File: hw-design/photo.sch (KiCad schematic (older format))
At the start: 10 parts, among them P6 CONN_01X17, P7 CONN_01X17, Q1 BC847, U2 TCS3472, U9 TCS3472

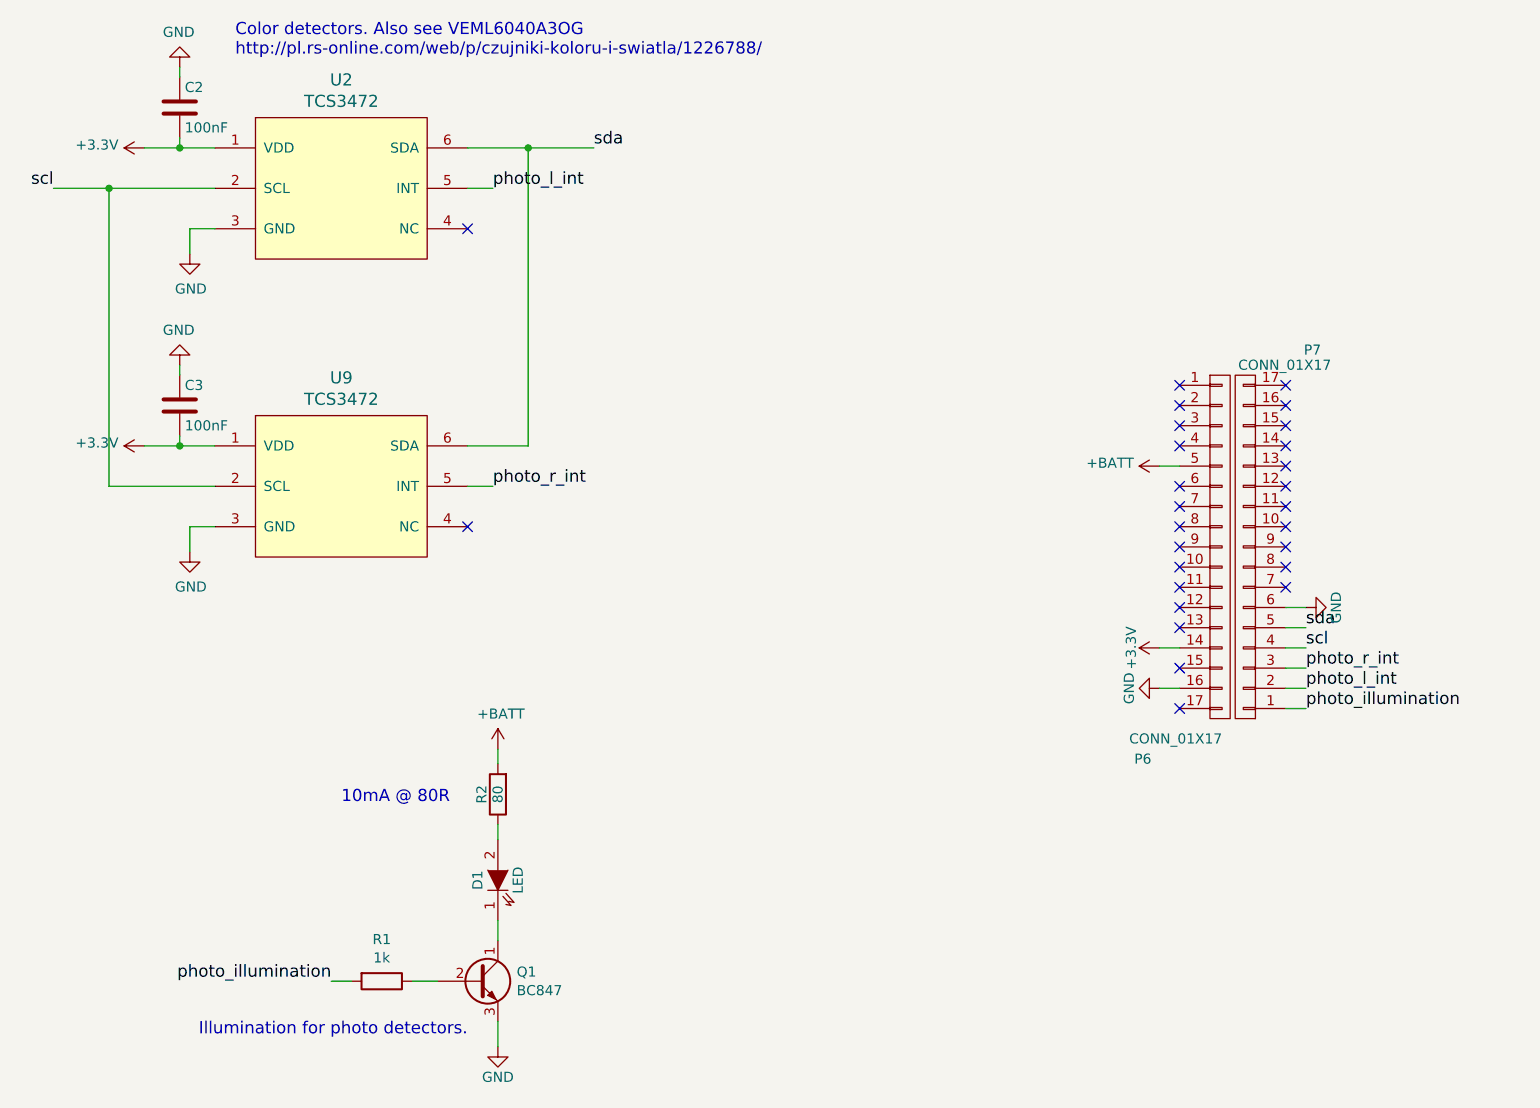
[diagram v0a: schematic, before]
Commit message: 2 boards and 1 little with color sensors.
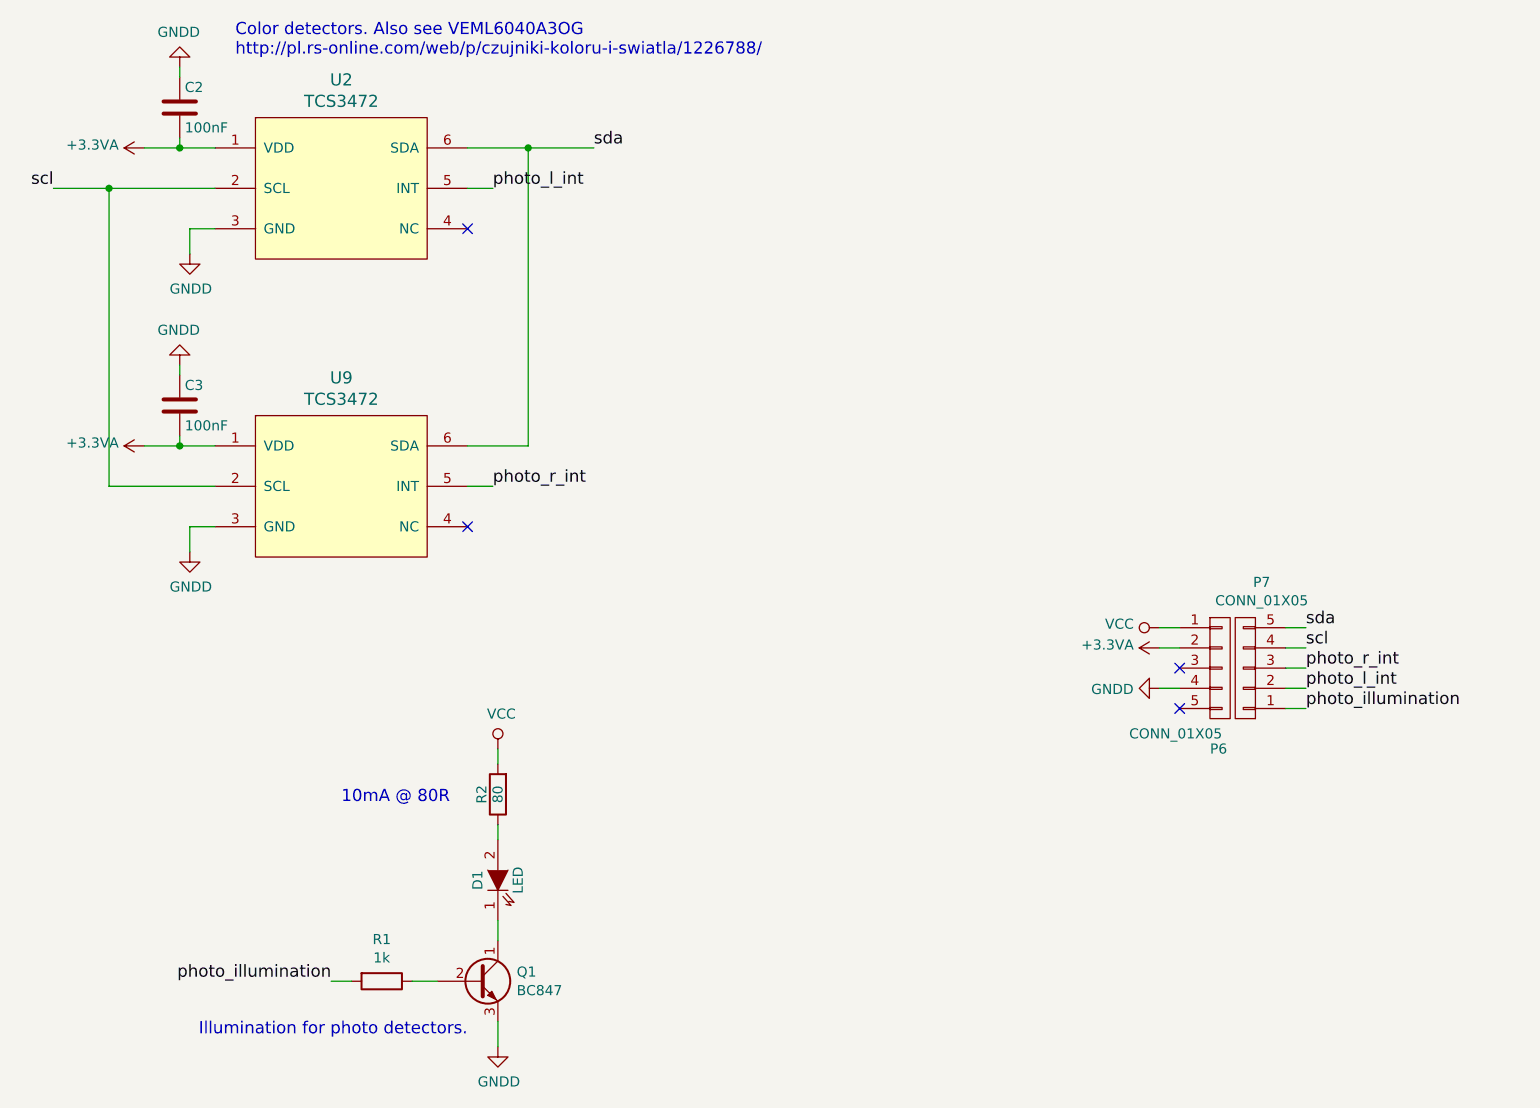
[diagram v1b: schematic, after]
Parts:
- removed P6, P7: CONN_01X17, iwasz:pin_socket_17, symbol CONN_01X17
- added P6, P7: CONN_01X05, w_pin_strip:pin_strip_5, symbol CONN_01X05
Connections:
- net photo_illumination: now also P7.1 (P1)
- net photo_l_int: now also P7.2 (P2)
- net photo_r_int: now also P7.3 (P3)
- net scl: now also P7.4 (P4)
- net sda: now also P7.5 (P5)
- net +3V3 renamed +3.3VA
- net +3.3VA: now also P6.2 (P2)
- net +BATT renamed VCC
- net VCC: now also P6.1 (P1)
- net GND renamed GNDD
- net GNDD: now also P6.4 (P4)
- no-connect marks 27 -> 4
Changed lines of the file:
@@
-	1    0    0    -1
-$EndComp
-$Comp
-L +3.3V #PWR72
-U 1 1 580FD812
-P 1625 1800
-F 0 "#PWR72" H 1625 1650 50  0001 C CNN
-F 1 "+3.3V" V 1640 1928 50  0000 L CNN
-F 2 "" H 1625 1800 50  0000 C CNN
-F 3 "" H 1625 1800 50  0000 C CNN
-	1    1625 1800
-	0    -1   -1   0
-$EndComp
-$Comp
-L GND #PWR74
-U 1 1 580FD818
-P 1800 1400
-F 0 "#PWR74" H 1800 1150 50  0001 C CNN
-F 1 "GND" H 1805 1227 50  0000 C CNN
-F 2 "" H 1800 1400 50  0000 C CNN
-F 3 "" H 1800 1400 50  0000 C CNN
-	1    1800 1400
-	-1   0    0    1
-$EndComp
-$Comp
-L GND #PWR76
-U 1 1 580FD81E
-P 1850 2325
-F 0 "#PWR76" H 1850 2075 50  0001 C CNN
-F 1 "GND" H 1855 2152 50  0000 C CNN
-F 2 "" H 1850 2325 50  0000 C CNN
-F 3 "" H 1850 2325 50  0000 C CNN
-	1    1850 2325
 	1    0    0    -1
 $EndComp
@@
 	1    0    0    -1
 $EndComp
-$Comp
-L +3.3V #PWR73
-U 1 1 580FD837
-P 1625 3275
-F 0 "#PWR73" H 1625 3125 50  0001 C CNN
-F 1 "+3.3V" V 1640 3403 50  0000 L CNN
-F 2 "" H 1625 3275 50  0000 C CNN
-F 3 "" H 1625 3275 50  0000 C CNN
-	1    1625 3275
-	0    -1   -1   0
-$EndComp
-$Comp
-L GND #PWR75
-U 1 1 580FD83D
-P 1800 2875
-F 0 "#PWR75" H 1800 2625 50  0001 C CNN
-F 1 "GND" H 1805 2702 50  0000 C CNN
-F 2 "" H 1800 2875 50  0000 C CNN
-F 3 "" H 1800 2875 50  0000 C CNN
-	1    1800 2875
-	-1   0    0    1
-$EndComp
-$Comp
-L GND #PWR77
-U 1 1 580FD843
-P 1850 3800
-F 0 "#PWR77" H 1850 3550 50  0001 C CNN
-F 1 "GND" H 1855 3627 50  0000 C CNN
-F 2 "" H 1850 3800 50  0000 C CNN
-F 3 "" H 1850 3800 50  0000 C CNN
-	1    1850 3800
-	1    0    0    -1
-$EndComp
 NoConn ~ 3225 3675
 $Comp
@@
 	-1   0    0    1
 $EndComp
-$Comp
-L GND #PWR79
-U 1 1 580FD859
-P 3375 6250
-F 0 "#PWR79" H 3375 6000 50  0001 C CNN
-F 1 "GND" H 3375 6100 50  0000 C CNN
-F 2 "" H 3375 6250 60  0000 C CNN
-F 3 "" H 3375 6250 60  0000 C CNN
-	1    3375 6250
-	1    0    0    -1
-$EndComp
 Text Notes 2075 1350 0    60   ~ 0
 Color detectors. Also see VEML6040A3OG\nhttp://pl.rs-online.com/web/p/czujniki-koloru-i-swiatla/1226788/
@@
 Wire Wire Line
 	2550 5925 2650 5925
-$Comp
-L +BATT #PWR78
-U 1 1 580FD88C
-P 3375 4775
-F 0 "#PWR78" H 3375 4625 50  0001 C CNN
-F 1 "+BATT" H 3390 4948 50  0000 C CNN
-F 2 "" H 3375 4775 50  0000 C CNN
-F 3 "" H 3375 4775 50  0000 C CNN
-	1    3375 4775
-	1    0    0    -1
-$EndComp
 Text Notes 2600 5050 0    60   ~ 0
 10mA @ 80R
-$Comp
-L GND #PWR82
-U 1 1 580FEB92
-P 6650 4475
-F 0 "#PWR82" H 6650 4225 50  0001 C CNN
-F 1 "GND" H 6650 4325 50  0000 C CNN
-F 2 "" H 6650 4475 60  0000 C CNN
-F 3 "" H 6650 4475 60  0000 C CNN
-	1    6650 4475
-	0    1    1    0
-$EndComp
-$Comp
-L +3.3V #PWR81
-U 1 1 580FEB98
-P 6650 4275
-F 0 "#PWR81" H 6650 4125 50  0001 C CNN
-F 1 "+3.3V" H 6650 4415 50  0000 C CNN
-F 2 "" H 6650 4275 60  0000 C CNN
-F 3 "" H 6650 4275 60  0000 C CNN
-	1    6650 4275
-	0    -1   -1   0
-$EndComp
-$Comp
-L +BATT #PWR80
-U 1 1 580FEB9E
-P 6650 3375
-F 0 "#PWR80" H 6650 3225 50  0001 C CNN
-F 1 "+BATT" V 6665 3502 50  0000 L CNN
-F 2 "" H 6650 3375 50  0000 C CNN
-F 3 "" H 6650 3375 50  0000 C CNN
-	1    6650 3375
-	0    -1   -1   0
-$EndComp
-$Comp
-L CONN_01X17 P6
-U 1 1 580FEBAA
-P 6950 3775
-F 0 "P6" H 6525 2725 50  0000 L CNN
-F 1 "CONN_01X17" H 6500 2825 50  0000 L CNN
-F 2 "iwasz:pin_socket_17" H 6950 3775 50  0001 C CNN
-F 3 "" H 6950 3775 50  0000 C CNN
-	1    6950 3775
-	1    0    0    -1
-$EndComp
-$Comp
-L CONN_01X17 P7
-U 1 1 580FEBB1
-P 7075 3775
-F 0 "P7" H 6700 2800 50  0000 L CNN
-F 1 "CONN_01X17" H 6650 2875 50  0000 L CNN
-F 2 "iwasz:pin_socket_17" H 7075 3775 50  0001 C CNN
-F 3 "" H 7075 3775 50  0000 C CNN
-	1    7075 3775
-	-1   0    0    1
-$EndComp
-$Comp
-L GND #PWR83
-U 1 1 580FEBB8
-P 7375 4075
-F 0 "#PWR83" H 7375 3825 50  0001 C CNN
-F 1 "GND" H 7375 3925 50  0000 C CNN
-F 2 "" H 7375 4075 60  0000 C CNN
-F 3 "" H 7375 4075 60  0000 C CNN
-	1    7375 4075
-	0    -1   -1   0
-$EndComp
 Wire Wire Line
 	7375 4575 7275 4575
@@
 	7275 4175 7375 4175
 Wire Wire Line
-	7375 4075 7275 4075
-Wire Wire Line
 	6650 4475 6750 4475
 Wire Wire Line
 	6650 4275 6750 4275
-Wire Wire Line
-	6650 3375 6750 3375
 Text Label 2550 5925 2    60   ~ 0
 photo_illumination
-NoConn ~ 7275 2975
-NoConn ~ 7275 3075
-NoConn ~ 7275 3175
-NoConn ~ 7275 3275
-NoConn ~ 7275 3375
-NoConn ~ 7275 3475
-NoConn ~ 7275 3575
-NoConn ~ 7275 3675
-NoConn ~ 7275 3775
-NoConn ~ 7275 3875
-NoConn ~ 7275 3975
-NoConn ~ 6750 2975
-NoConn ~ 6750 3075
-NoConn ~ 6750 3175
-NoConn ~ 6750 3275
-NoConn ~ 6750 3475
-NoConn ~ 6750 3575
-NoConn ~ 6750 3675
-NoConn ~ 6750 3775
-NoConn ~ 6750 3875
-NoConn ~ 6750 3975
-NoConn ~ 6750 4075
-NoConn ~ 6750 4175
 NoConn ~ 6750 4375
 NoConn ~ 6750 4575
@@
 Text Label 3850 1800 0    60   ~ 0
 sda
+Wire Wire Line
+	6650 4175 6750 4175
+$Comp
+L CONN_01X05 P6
+U 1 1 58107EC9
+P 6950 4375
+F 0 "P6" H 6900 3975 50  0000 L CNN
+F 1 "CONN_01X05" H 6500 4050 50  0000 L CNN
+F 2 "w_pin_strip:pin_strip_5" H 6950 4375 50  0001 C CNN
+F 3 "" H 6950 4375 50  0000 C CNN
+	1    6950 4375
+	1    0    0    -1
+$EndComp
+$Comp
+L CONN_01X05 P7
+U 1 1 58107F52
+P 7075 4375
+F 0 "P7" H 6994 3950 50  0000 C CNN
+F 1 "CONN_01X05" H 6994 4041 50  0000 C CNN
+F 2 "w_pin_strip:pin_strip_5" H 7075 4375 50  0001 C CNN
+F 3 "" H 7075 4375 50  0000 C CNN
+	1    7075 4375
+	-1   0    0    1
+$EndComp
+$Comp
+L GNDD #PWR072
+U 1 1 5810AACC
+P 6650 4475
+F 0 "#PWR072" H 6650 4225 50  0001 C CNN
+F 1 "GNDD" V 6655 4347 50  0000 R CNN
+F 2 "" H 6650 4475 50  0000 C CNN
+F 3 "" H 6650 4475 50  0000 C CNN
+	1    6650 4475
+	0    1    1    0
+$EndComp
+$Comp
+L GNDD #PWR073
+U 1 1 5810ACB5
+P 3375 6250
+F 0 "#PWR073" H 3375 6000 50  0001 C CNN
+F 1 "GNDD" H 3380 6077 50  0000 C CNN
+F 2 "" H 3375 6250 50  0000 C CNN
+F 3 "" H 3375 6250 50  0000 C CNN
+	1    3375 6250
+	1    0    0    -1
+$EndComp
+$Comp
+L GNDD #PWR074
+U 1 1 5810AE79
+P 1850 3800
+F 0 "#PWR074" H 1850 3550 50  0001 C CNN
+F 1 "GNDD" H 1855 3627 50  0000 C CNN
+F 2 "" H 1850 3800 50  0000 C CNN
+F 3 "" H 1850 3800 50  0000 C CNN
+	1    1850 3800
+	1    0    0    -1
+$EndComp
+$Comp
+L GNDD #PWR075
+U 1 1 5810B1A5
+P 1850 2325
+F 0 "#PWR075" H 1850 2075 50  0001 C CNN
+F 1 "GNDD" H 1855 2152 50  0000 C CNN
+F 2 "" H 1850 2325 50  0000 C CNN
+F 3 "" H 1850 2325 50  0000 C CNN
+	1    1850 2325
+	1    0    0    -1
+$EndComp
+$Comp
+L GNDD #PWR076
+U 1 1 5810BAE3
+P 1800 1400
+F 0 "#PWR076" H 1800 1150 50  0001 C CNN
+F 1 "GNDD" H 1805 1227 50  0000 C CNN
+F 2 "" H 1800 1400 50  0000 C CNN
+F 3 "" H 1800 1400 50  0000 C CNN
+	1    1800 1400
+	-1   0    0    1
+$EndComp
+$Comp
+L GNDD #PWR077
+U 1 1 5810BB3E
+P 1800 2875
+F 0 "#PWR077" H 1800 2625 50  0001 C CNN
+F 1 "GNDD" H 1805 2702 50  0000 C CNN
+F 2 "" H 1800 2875 50  0000 C CNN
+F 3 "" H 1800 2875 50  0000 C CNN
+	1    1800 2875
+	-1   0    0    1
+$EndComp
+$Comp
+L +3.3VA #PWR078
+U 1 1 5810C31D
+P 6650 4275
+F 0 "#PWR078" H 6650 4125 50  0001 C CNN
+F 1 "+3.3VA" V 6665 4402 50  0000 L CNN
+F 2 "" H 6650 4275 50  0000 C CNN
+F 3 "" H 6650 4275 50  0000 C CNN
+	1    6650 4275
+	0    -1   -1   0
+$EndComp
+$Comp
+L +3.3VA #PWR079
+U 1 1 5810C3D0
+P 1625 1800
+F 0 "#PWR079" H 1625 1650 50  0001 C CNN
+F 1 "+3.3VA" V 1640 1927 50  0000 L CNN
+F 2 "" H 1625 1800 50  0000 C CNN
+F 3 "" H 1625 1800 50  0000 C CNN
+	1    1625 1800
+	0    -1   -1   0
+$EndComp
+$Comp
+L +3.3VA #PWR080
+U 1 1 5810C788
+P 1625 3275
+F 0 "#PWR080" H 1625 3125 50  0001 C CNN
+F 1 "+3.3VA" V 1640 3402 50  0000 L CNN
+F 2 "" H 1625 3275 50  0000 C CNN
+F 3 "" H 1625 3275 50  0000 C CNN
+	1    1625 3275
+	0    -1   -1   0
+$EndComp
+$Comp
+L VCC #PWR081
+U 1 1 5810D785
+P 6650 4175
+F 0 "#PWR081" H 6650 4025 50  0001 C CNN
+F 1 "VCC" V 6668 4302 50  0000 L CNN
+F 2 "" H 6650 4175 50  0000 C CNN
+F 3 "" H 6650 4175 50  0000 C CNN
+	1    6650 4175
+	0    -1   -1   0
+$EndComp
+$Comp
+L VCC #PWR082
+U 1 1 5810D81A
+P 3375 4775
+F 0 "#PWR082" H 3375 4625 50  0001 C CNN
+F 1 "VCC" H 3392 4948 50  0000 C CNN
+F 2 "" H 3375 4775 50  0000 C CNN
+F 3 "" H 3375 4775 50  0000 C CNN
+	1    3375 4775
+	1    0    0    -1
+$EndComp
 $EndSCHEMATC
